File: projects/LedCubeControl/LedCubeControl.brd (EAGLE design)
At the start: 30.1 x 69.8 mm, 29 parts, among them IC1 74HC595N, IC2 74HC595N, IC3 74HC595N, T1 PN2222A, T2 PN2222A, T3 PN2222A, T4 PN2222A

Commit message: fix: small fixes applied
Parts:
- moved R2 10.2 mm to (11.4, 64.8)
- moved IC1 10.2 mm to (22.9, 57.1)
- moved IC2 10.2 mm to (22.9, 34.3)
- moved R11 10.2 mm to (11.4, 41.9)
- moved R12 10.2 mm to (11.4, 39.4)
- moved R13 10.2 mm to (11.4, 36.8)
- moved R14 10.2 mm to (11.4, 34.3)
- moved R3 10.2 mm to (11.4, 62.2)
- moved R5 10.2 mm to (11.4, 57.1)
- moved SV2 10.2 mm to (3.81, 43.2)
- moved T3 10.2 mm to (6.35, 6.35)
- moved T4 10.2 mm to (14.0, 6.35)
- moved IC3 10.2 mm to (22.9, 11.4)
- moved R18 10.2 mm to (11.4, 24.1)
- moved R19 10.2 mm to (11.4, 21.6)
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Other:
- board size 30.1 x 69.8 mm -> 30.5 x 69.8 mm

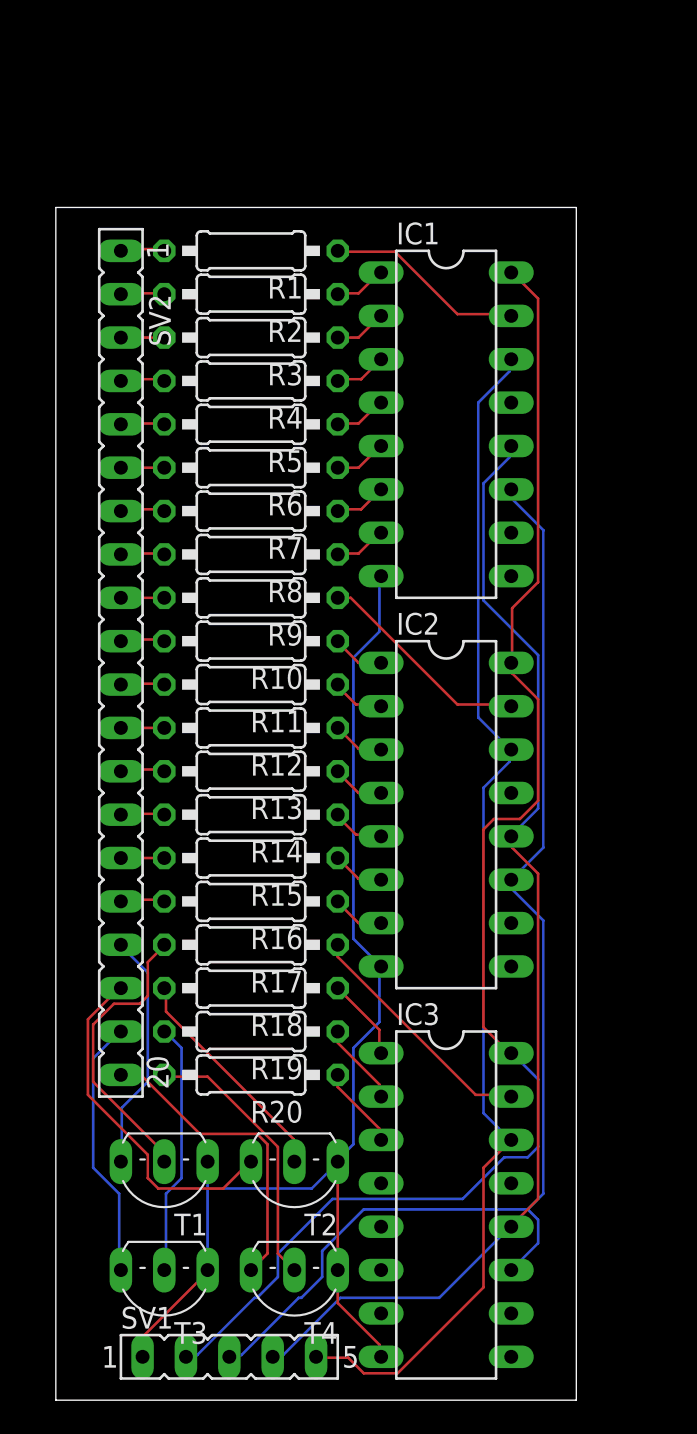
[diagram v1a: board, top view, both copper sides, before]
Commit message: fix: led control layout fixed
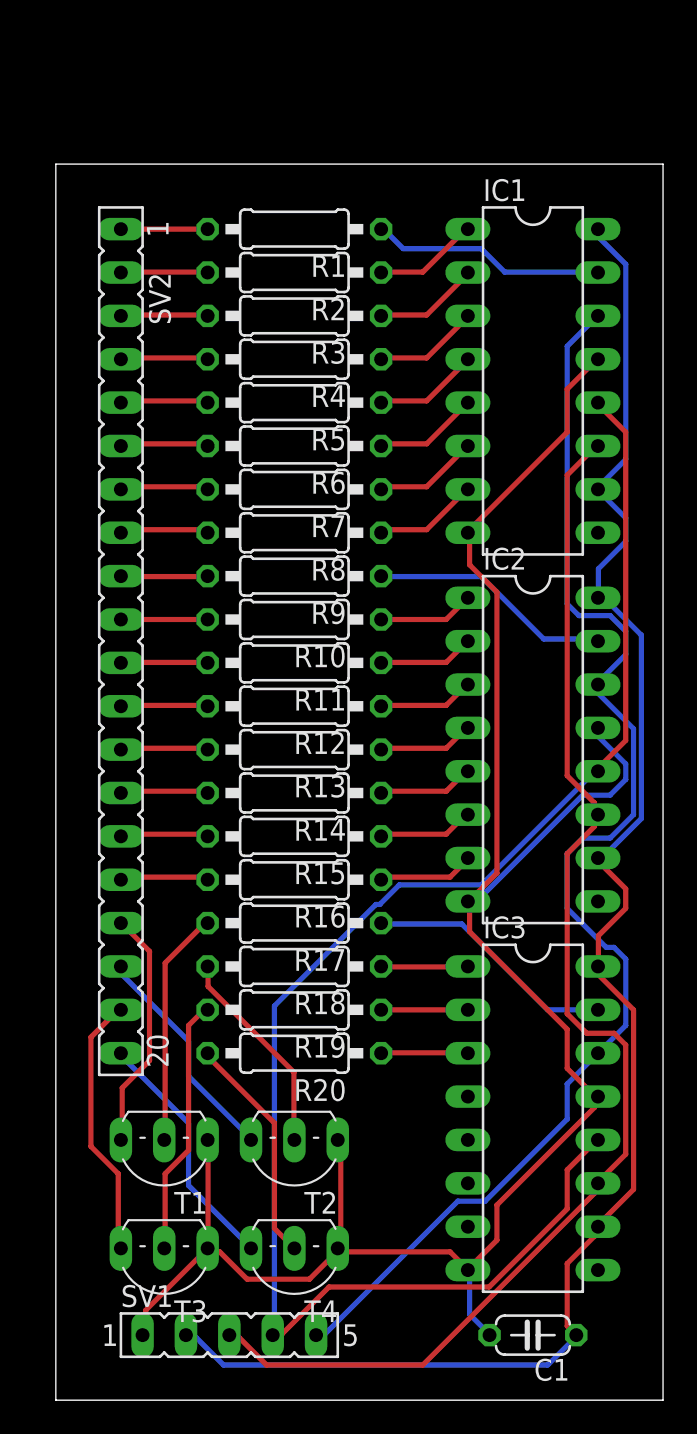
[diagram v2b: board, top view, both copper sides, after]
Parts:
- added C1: 1µF, rcl:C050-024X044
- moved IC3 7.18 mm to (27.9, 16.5)
- moved IC2 6.35 mm to (27.9, 38.1)
- moved IC1 5.68 mm to (27.9, 59.7)
- moved R2 2.84 mm to (14.0, 66.0)
- moved R11 2.84 mm to (14.0, 43.2)
- moved R12 2.84 mm to (14.0, 40.6)
- moved R13 2.84 mm to (14.0, 38.1)
- moved R14 2.84 mm to (14.0, 35.6)
- moved R15 2.84 mm to (14.0, 33.0)
- moved R3 2.84 mm to (14.0, 63.5)
- moved R4 2.84 mm to (14.0, 61.0)
- moved R5 2.84 mm to (14.0, 58.4)
- moved R6 2.84 mm to (14.0, 55.9)
- moved R7 2.84 mm to (14.0, 53.3)
- moved R16 2.84 mm to (14.0, 30.5)
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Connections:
- net GND: now also C1.2, IC1.13, IC2.13, IC3.13
- net VCC: now also C1.1, IC1.10, IC2.10, IC3.10
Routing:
- net GND: track 70.5 -> 121.6 mm
- net N$3: track 66.9 -> 92.0 mm
- net VCC: track 83.4 -> 98.6 mm
- net N$2: track 70.3 -> 77.4 mm
- net N$41: track 20.4 -> 13.3 mm
- net N$1: track 71.3 -> 75.5 mm
- net N$46: track 18.1 -> 14.6 mm
- net N$37: track 17.0 -> 13.8 mm
- net N$27: track 3.06 -> 6.15 mm
- net N$29: track 3.06 -> 6.13 mm
- net N$31: track 3.10 -> 6.13 mm
- net N$28: track 3.10 -> 6.13 mm
- net N$25: track 3.10 -> 6.12 mm
- net N$26: track 3.13 -> 6.14 mm
- net N$30: track 3.13 -> 6.13 mm
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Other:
- board size 30.5 x 69.8 mm -> 35.6 x 72.4 mm

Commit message: fix: capacitor value fixed
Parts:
- C1: value 1µF -> 10µF
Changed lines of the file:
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@@
 <attribute name="VALUE" x="16.51" y="12.192" size="1.27" layer="27" ratio="10" rot="R180"/>
 </element>
-<element name="C1" library="rcl" library_urn="urn:adsk.eagle:library:334" package="C050-024X044" package3d_urn="urn:adsk.eagle:package:23643/1" value="1µF" x="27.94" y="3.81" smashed="yes" rot="R180">
+<element name="C1" library="rcl" library_urn="urn:adsk.eagle:library:334" package="C050-024X044" package3d_urn="urn:adsk.eagle:package:23643/1" value="10µF" x="27.94" y="3.81" smashed="yes" rot="R180">
 <attribute name="NAME" x="30.099" y="2.413" size="1.27" layer="25" ratio="10" rot="R180"/>
 <attribute name="POPULARITY" value="33" x="27.94" y="3.81" size="1.778" layer="27" rot="R180" display="off"/>

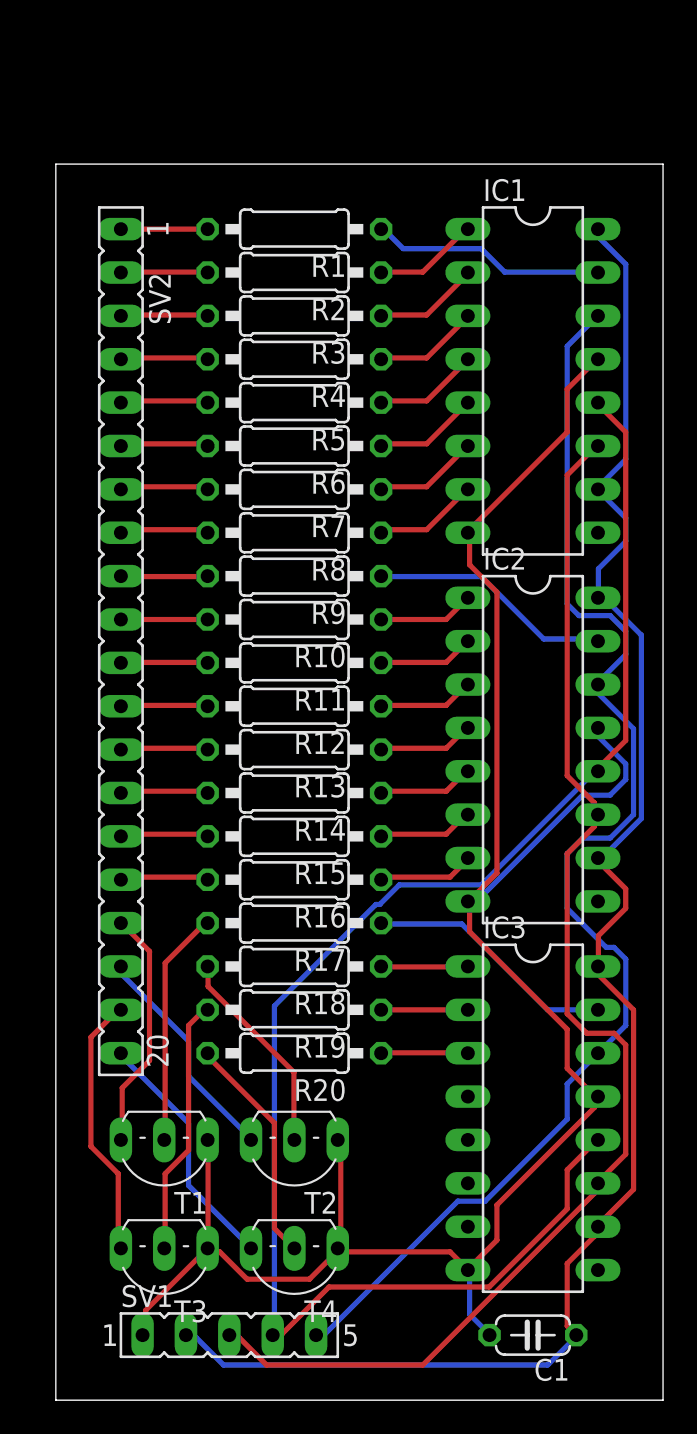
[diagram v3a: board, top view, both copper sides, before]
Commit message: fix: mwrt and led control fixed
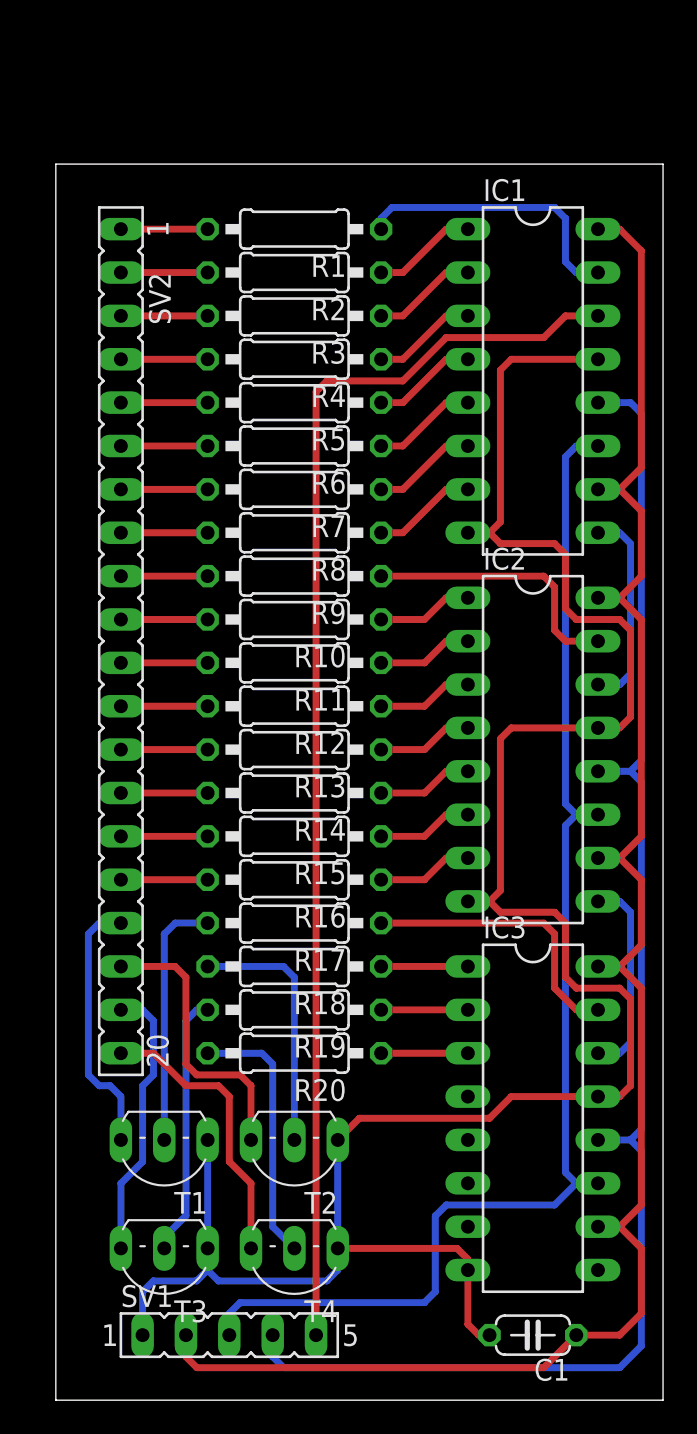
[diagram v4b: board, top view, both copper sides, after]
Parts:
- R1, R10, R11, R12, R13, R14, R15, R16, R2, R3, R4, R5, R6, R7, R8, R9: value 220 -> 39
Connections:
- new net N$48: IC1.14, SV1.5
- new net N$49: IC2.9, IC3.14
- net N$2: now also IC1.9; no longer IC1.14, IC3.14, SV1.5
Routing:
- net N$48: track 0.00 -> 73.6 mm
- net N$2: track 77.4 -> 12.0 mm
- net N$49: track 0.00 -> 12.0 mm
- net GND: track 121.6 -> 133.3 mm
- net VCC: track 98.6 -> 106.4 mm
- net N$3: track 92.0 -> 85.9 mm
- net N$41: track 13.3 -> 16.7 mm
- net N$24: track 13.7 -> 16.7 mm
- net N$40: track 12.3 -> 14.9 mm
- net N$46: track 14.6 -> 16.8 mm
- net N$36: track 14.8 -> 16.7 mm
- net N$47: track 13.5 -> 15.4 mm
- net N$35: track 14.3 -> 15.8 mm
- net N$38: track 14.1 -> 15.4 mm
- net N$37: track 13.8 -> 14.9 mm
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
